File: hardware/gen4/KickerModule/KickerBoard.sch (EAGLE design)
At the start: 108 parts

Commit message: mainboard placement
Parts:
- C14, C6: value 1000uF -> 1500uF
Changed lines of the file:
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@@
 <part name="GND_TEST" library="gen3" deviceset="TEST_PT" device=""/>
 <part name="12VGND_TEST" library="gen3" deviceset="TEST_PT" device=""/>
-<part name="C6" library="rcl" deviceset="CPOL-US" device="E10-35" value="1000uF"/>
-<part name="C14" library="rcl" deviceset="CPOL-US" device="E10-35" value="1000uF"/>
+<part name="C6" library="rcl" deviceset="CPOL-US" device="E10-35" value="1500uF"/>
+<part name="C14" library="rcl" deviceset="CPOL-US" device="E10-35" value="1500uF"/>
 <part name="NEON" library="pinhead" deviceset="PINHD-1X2" device=""/>
 <part name="R24" library="SparkFun-Passives" deviceset="RESISTOR" device="0805-RES" value="536k"/>

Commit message: main board in progress - about two thirds
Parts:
- removed BATCLAMP1: DIODE-ZENERDO214AC, gen3:DIODE-ZENERDO214AC
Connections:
- removed net 5V: BATCLAMP1.C
- removed net N$16: R16.2, U$2.DRAIN
- net AND_KICK: now also U$4.IN+
- net BATSENSE: no longer BATCLAMP1.A
- net CAP+: now also R16.2; no longer R16.1
- net DISCHARGE: no longer COM_BOARD.18
- net DRIB: now also COM_BOARD.18
- net N$10: now also R16.1, U$2.DRAIN; no longer U$4.IN+
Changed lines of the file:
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@@
 <part name="R18" library="SparkFun-Passives" deviceset="RESISTOR" device="0805-RES" value="20k"/>
 <part name="12V_TEST" library="gen3" deviceset="TEST_PT" device=""/>
-<part name="BATCLAMP1" library="gen3" deviceset="DIODE-ZENER" device="DO214AC" value="DIODE-ZENERDO214AC"/>
 <part name="BATCLAMP2" library="gen3" deviceset="DIODE-ZENER" device="DO214AC" value="DIODE-ZENERDO214AC"/>
 <part name="DRIB_TRAN" library="gen3" deviceset="N-MOSFET" device="DPAK"/>
@@
 <instance part="R18" gate="G$1" x="556.26" y="269.24" rot="R90"/>
 <instance part="12V_TEST" gate="G$1" x="403.86" y="358.14"/>
-<instance part="BATCLAMP1" gate="G$1" x="543.56" y="281.94" smashed="yes" rot="R90">
-<attribute name="NAME" x="540.5374" y="279.4" size="1.778" layer="95" rot="R90"/>
-</instance>
 <instance part="BATCLAMP2" gate="G$1" x="543.56" y="271.78" smashed="yes" rot="R90">
 <attribute name="NAME" x="540.5374" y="261.62" size="1.778" layer="95" rot="R90"/>
@@
 <instance part="U$2" gate="G$1" x="543.56" y="327.66"/>
 <instance part="R3" gate="G$1" x="532.13" y="323.85"/>
-<instance part="R16" gate="G$1" x="546.1" y="337.82"/>
+<instance part="R16" gate="G$1" x="546.1" y="337.82" rot="R180"/>
 <instance part="R22" gate="G$1" x="581.66" y="337.82"/>
 <instance part="U$5" gate="G$1" x="574.04" y="312.42"/>
@@
 <segment>
 <label x="561.34" y="347.98" size="1.778" layer="95"/>
-<pinref part="R16" gate="G$1" pin="1"/>
 <pinref part="R22" gate="G$1" pin="1"/>
-<wire x1="546.1" y1="342.9" x2="563.88" y2="342.9" width="0.1524" layer="91"/>
 <wire x1="563.88" y1="342.9" x2="581.66" y2="342.9" width="0.1524" layer="91"/>
 <wire x1="563.88" y1="342.9" x2="563.88" y2="347.98" width="0.1524" layer="91"/>
+<pinref part="R16" gate="G$1" pin="2"/>
+<wire x1="563.88" y1="342.9" x2="546.1" y2="342.9" width="0.1524" layer="91"/>
 <junction x="563.88" y="342.9"/>
 </segment>
@@
 <wire x1="383.54" y1="297.18" x2="383.54" y2="302.26" width="0.1524" layer="91"/>
 <junction x="383.54" y="302.26"/>
+</segment>
+<segment>
+<pinref part="U$4" gate="G$1" pin="IN+"/>
+<wire x1="431.8" y1="302.26" x2="403.86" y2="302.26" width="0.1524" layer="91"/>
 </segment>
 </net>
@@
 </segment>
 </net>
-<net name="N$10" class="0">
-<segment>
-<pinref part="U$4" gate="G$1" pin="IN+"/>
-<wire x1="431.8" y1="302.26" x2="403.86" y2="302.26" width="0.1524" layer="91"/>
-</segment>
-</net>
 <net name="N$5" class="0">
 <segment>
@@
 </net>
 <net name="DISCHARGE" class="0">
-<segment>
-<pinref part="COM_BOARD" gate="G$1" pin="18"/>
-<wire x1="383.54" y1="228.6" x2="393.7" y2="228.6" width="0.1524" layer="91"/>
-<junction x="383.54" y="228.6"/>
-</segment>
 <segment>
 <pinref part="COM_BOARD" gate="G$1" pin="16"/>
@@
 <wire x1="543.56" y1="276.86" x2="533.4" y2="276.86" width="0.1524" layer="91"/>
 <wire x1="543.56" y1="274.32" x2="543.56" y2="276.86" width="0.1524" layer="91"/>
-<pinref part="BATCLAMP1" gate="G$1" pin="A"/>
-<wire x1="543.56" y1="279.4" x2="543.56" y2="276.86" width="0.1524" layer="91"/>
 <pinref part="BATSENSE_TEST" gate="G$1" pin="P$1"/>
 <junction x="548.64" y="276.86"/>
 <junction x="556.26" y="276.86"/>
 <junction x="543.56" y="276.86"/>
-</segment>
-</net>
-<net name="5V" class="0">
-<segment>
-<pinref part="BATCLAMP1" gate="G$1" pin="C"/>
-<wire x1="543.56" y1="284.48" x2="543.56" y2="287.02" width="0.1524" layer="91"/>
-<label x="543.56" y="287.02" size="1.778" layer="95"/>
 </segment>
 </net>
@@
 <junction x="289.56" y="350.52"/>
 <label x="386.08" y="228.6" size="1.778" layer="95"/>
+</segment>
+<segment>
+<pinref part="COM_BOARD" gate="G$1" pin="18"/>
+<wire x1="383.54" y1="228.6" x2="393.7" y2="228.6" width="0.1524" layer="91"/>
 </segment>
 </net>
@@
 </segment>
 </net>
-<net name="N$16" class="0">
-<segment>
-<wire x1="546.1" y1="332.74" x2="546.1" y2="331.978" width="0.1524" layer="91"/>
-<pinref part="U$2" gate="G$1" pin="DRAIN"/>
-<pinref part="R16" gate="G$1" pin="2"/>
-</segment>
-</net>
 <net name="N$18" class="0">
 <segment>
@@
 </segment>
 </net>
+<net name="N$10" class="0">
+<segment>
+<pinref part="U$2" gate="G$1" pin="DRAIN"/>
+<wire x1="546.1" y1="331.978" x2="546.1" y2="332.74" width="0.1524" layer="91"/>
+<pinref part="R16" gate="G$1" pin="1"/>
+</segment>
+</net>

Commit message: So close - few traces left
should be done tommorow
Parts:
- added KICKER1: (no value), fuse:TR5
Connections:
- new net 12V-KICKER: C18.1, C20.1, C21.1, C23.1, CHARGE_U.VCC, CHARGE_U.VT, KICKER1.2, U$3.P$4, U$3.P$5
- net 12V: now also KICKER1.1; no longer C18.1, C20.1, C21.1, C23.1, CHARGE_U.VCC, CHARGE_U.VT, U$3.P$4, U$3.P$5
- net N$26: now also MOTOR2.1, MOTOR2.3
- net N$4: now also MOTOR3.1, MOTOR3.3

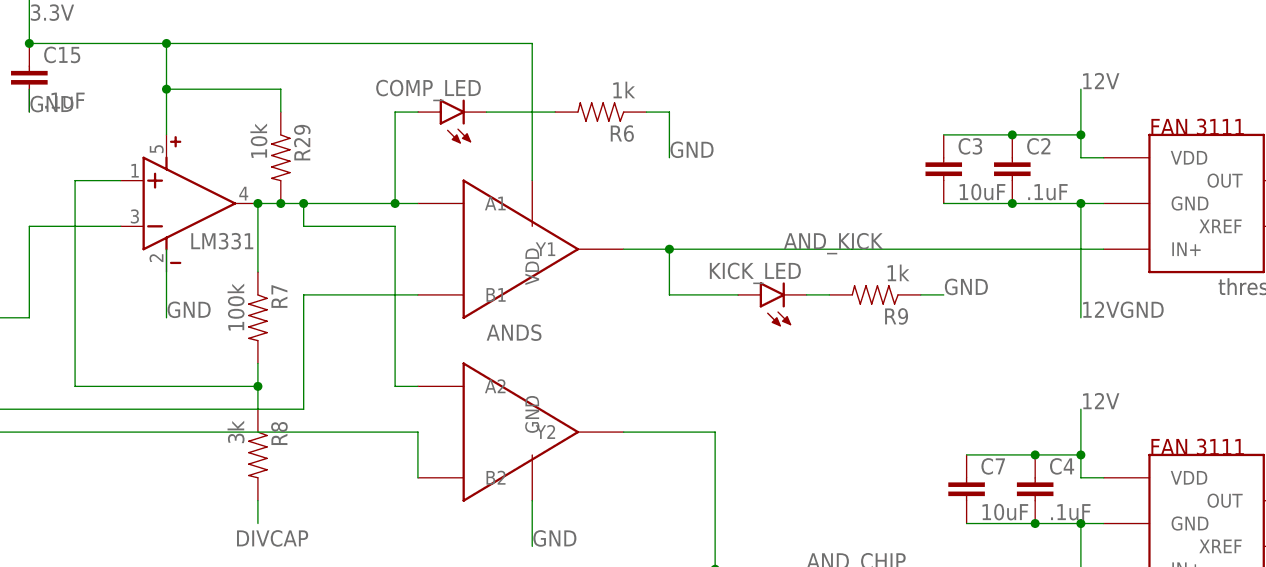
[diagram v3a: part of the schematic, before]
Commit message: few fixes
unconnected wires
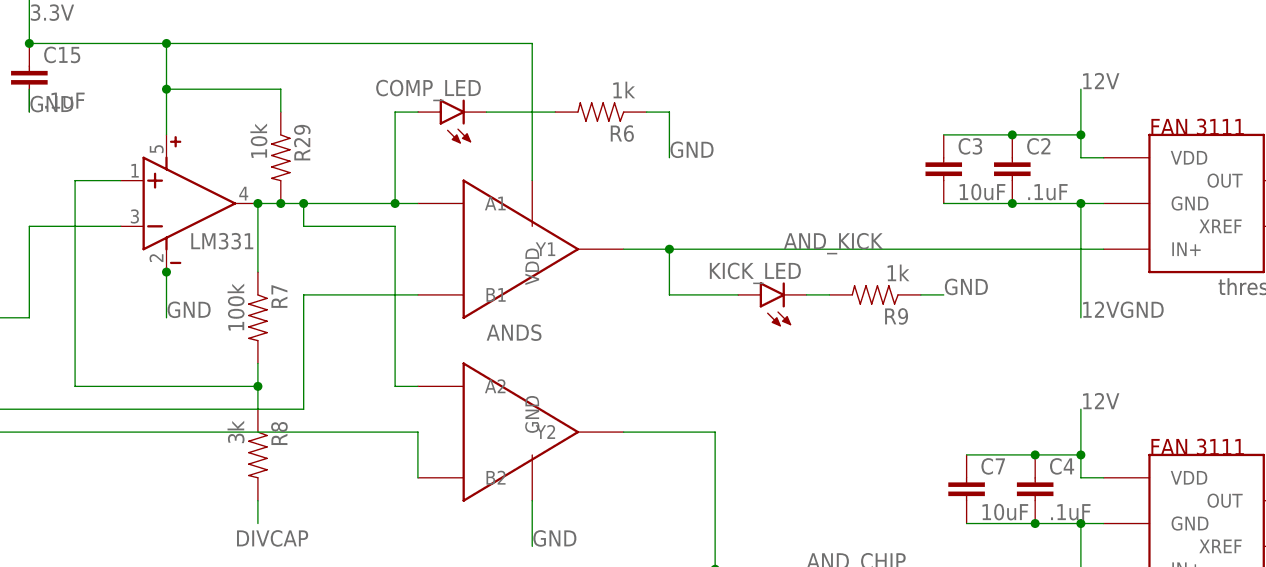
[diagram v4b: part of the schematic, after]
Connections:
- net GND: now also CAP_COMP.V-
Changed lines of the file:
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@@
 </segment>
 <segment>
-<wire x1="327.66" y1="302.26" x2="327.66" y2="294.64" width="0.1524" layer="91"/>
+<wire x1="327.66" y1="299.72" x2="327.66" y2="294.64" width="0.1524" layer="91"/>
 <label x="327.66" y="294.64" size="1.778" layer="95"/>
+<pinref part="CAP_COMP" gate="G$1" pin="V-"/>
+<junction x="327.66" y="299.72"/>
 </segment>
 <segment>
@@
 <label x="396.24" y="302.26" size="1.778" layer="95"/>
 <pinref part="KICK_LED" gate="G$1" pin="A"/>
-<wire x1="383.54" y1="302.26" x2="403.86" y2="302.26" width="0.1524" layer="91"/>
 <wire x1="391.16" y1="297.18" x2="383.54" y2="297.18" width="0.1524" layer="91"/>
 <wire x1="383.54" y1="297.18" x2="383.54" y2="302.26" width="0.1524" layer="91"/>
 <junction x="383.54" y="302.26"/>
-</segment>
-<segment>
 <pinref part="U$4" gate="G$1" pin="IN+"/>
-<wire x1="431.8" y1="302.26" x2="403.86" y2="302.26" width="0.1524" layer="91"/>
+<wire x1="383.54" y1="302.26" x2="431.8" y2="302.26" width="0.1524" layer="91"/>
 </segment>
 </net>
@@
 </sheet>
 </sheets>
-<errors>
-</errors>
 </schematic>
 </drawing>

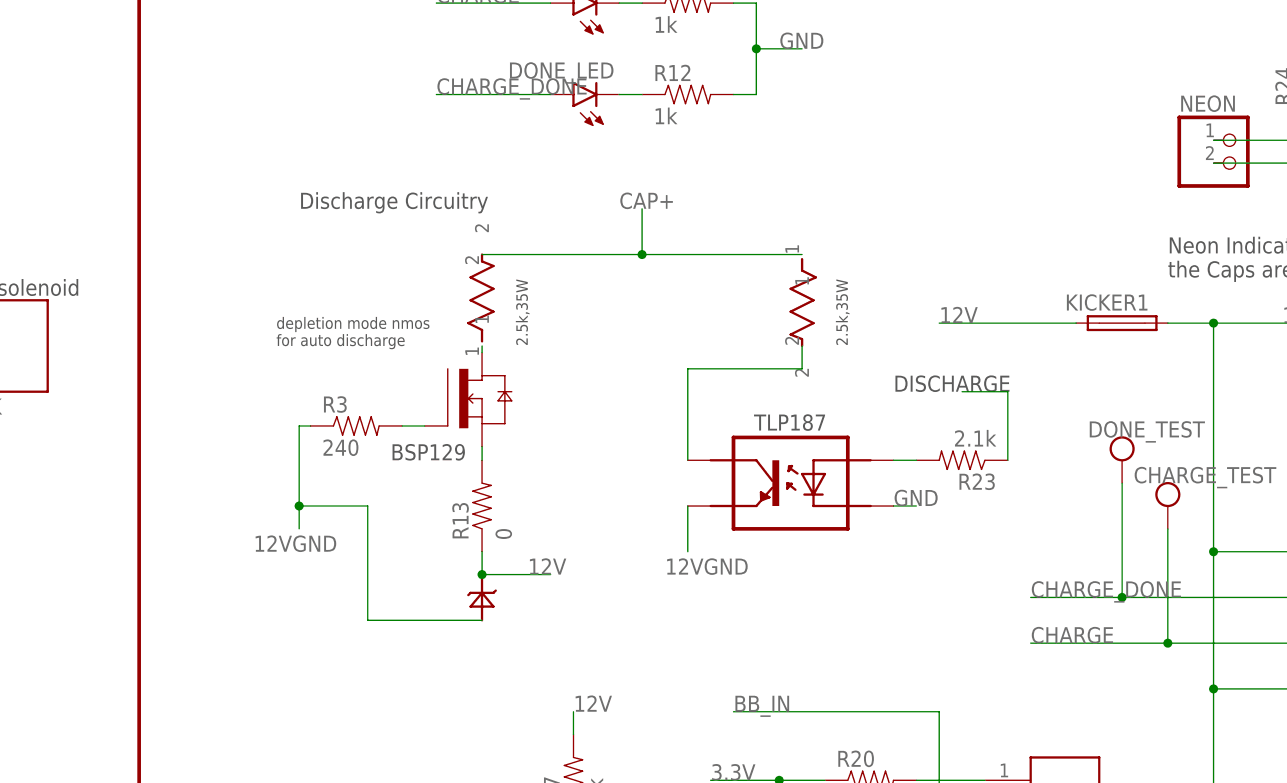
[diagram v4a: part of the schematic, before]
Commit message: updated auto discharge - need manual discharge
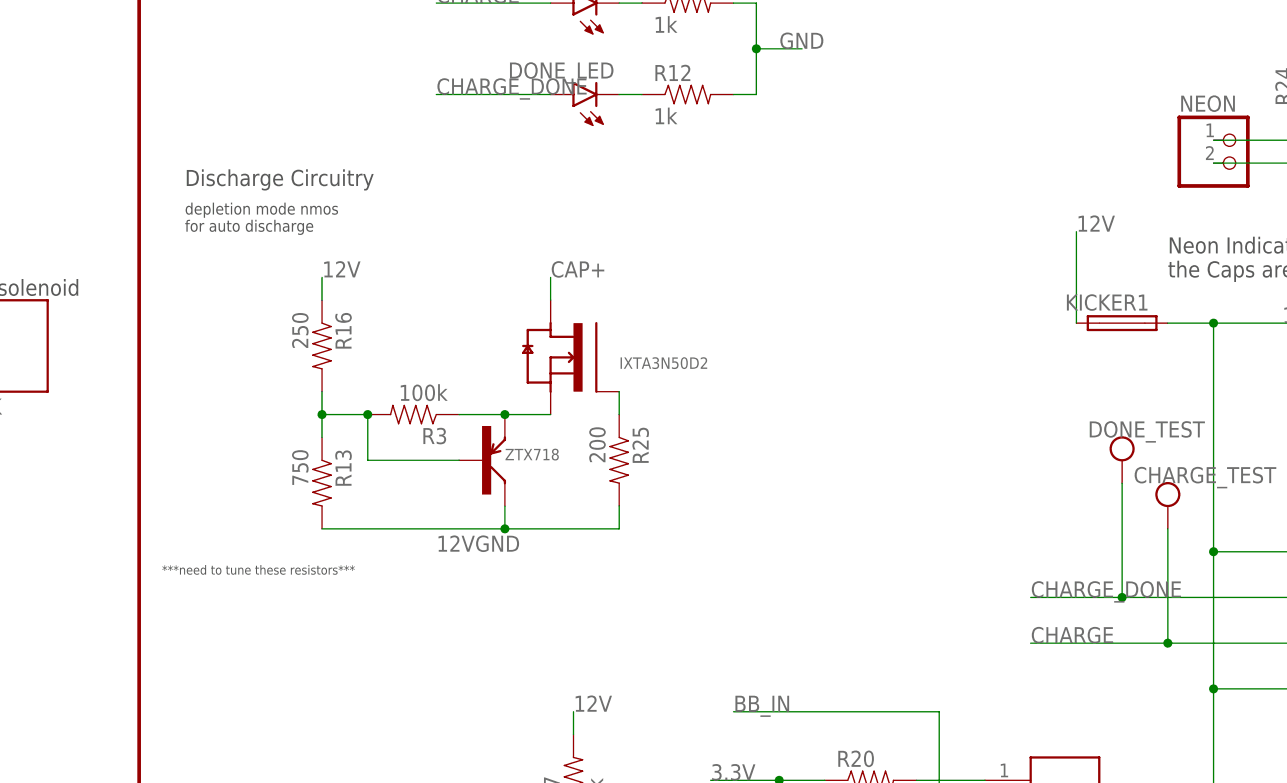
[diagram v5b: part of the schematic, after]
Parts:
- removed R22: POWRESISTOR, rfc:POWRESISTOR
- removed R23: 2.1k, SparkFun-Passives:RESISTOR0805-RES
- removed U$5: TLP187, rfc:TLP187
- added R25: 200, SparkFun-Passives:RESISTOR0805-RES
- R13: value 0 -> 750
- R16: value POWRESISTOR -> 250; device rfc:POWRESISTOR -> SparkFun-Passives:RESISTOR0805-RES
- R3: value 240 -> 100k
- U$2: value BSP129-NMOS_DEPLETION -> IXTA3N50D2; device kickerchips:BSP129-NMOS_DEPLETION -> rfc:IXTA3N50D2
- U$6: value 13VZENER -> ZTX718; device rfc:13VZENER -> rfc:ZTX718
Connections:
- removed net N$29: R22.2, U$5.DRAIN
- removed net N$30: R23.2, U$5.DIODE+
- net 12V: now also R16.1; no longer R13.1, U$6.-
- net 12VGND: now also R13.2, R25.2, U$6.COLLECTOR; no longer R3.1, U$5.SOURCE, U$6.+
- net CAP+: now also U$2.DRAIN; no longer R16.2, R22.1
- net DISCHARGE: no longer R23.1
- net GND: no longer U$5.DIODE-
- net N$10: now also R3.1, U$2.SOURCE, U$6.EMITTER; no longer R16.1, U$2.DRAIN
- net N$18: now also R13.1, R16.2, U$6.BASE; no longer U$2.GATE
- net N$21: now also R25.1, U$2.GATE; no longer R13.2, U$2.SOURCE
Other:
- note added: "***need to tune these resistors***"
- note added: "IXTA3N50D2"
- note added: "ZTX718"
- note removed: "2.5k,35W"
- note removed: "BSP129"
- note removed: "TLP187"
- moved on the sheet: R13, R3
